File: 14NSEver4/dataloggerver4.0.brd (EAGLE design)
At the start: 80 x 25.4 mm, 44 parts, among them Q1 16mhz, SW2 SRIDE_SWITCH

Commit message: changed board files
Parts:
- removed C7: 3.3uF, rcl:C0603
- removed CON1, CON3: (no value), XR Connector:3PIN
- removed CON2, CON4, CON5: (no value), XR Connector:2PIN
- removed D1, D2: (no value), ChipDiodes:SOD-123
- removed DCDC1, DCDC3: (no value), DC-DC:5V1A_M78AR05-1
- removed DCDC2: (no value), DC-DC:3.3V1A_M78AR033-1
- removed IM2: IM920_IM920C, CANSAT12th:IM920_IM920C
- removed U$2, U$4, U$5: 2SJ681-PCH, mosfet:2SJ681
- removed U$6, U$7: 1X5, PinSocket:1X5
- removed U$8: ATMEGA328P-AU, ATMEGA328P-AU:QFP80P900X900X120-32N
- added BMX1, BMX2: BMX055, BMX055:BMX055
- added CN1, CN2: DM3AT, microSD:DM3AT
- added JP3, JP5, JP7: (no value), pinhead:1X05
- added JP4, JP6: (no value), pinhead:1X06
- added L3, L4: (no value), Chip LED:OSXX1608C1A
- added Q2: 16mhz, crystal:HC49UP
- added R16, R17, R18, R2, R3, R5, R6: 10k, rcl:R0603
- added U$1: ATMEGA328P-AU, ATMAGA328P-AU:QFP80P900X900X120-32N
- C4: value 3.3uF -> 22p
- C5: value 10uF -> 22p
- C6: value 3.3uF -> 0.1μ
- R10, R8: value 1k -> 10k
- R14, R15: value 4.7k -> 100
- R9: value 100k -> 10k
- SW2: value SRIDE_SWITCH -> (none); device Sride Switch:SRIDE_SWITCH -> Tact switch:TVAF06-A020B-R
- U$3: value 2SK4017-NCH -> ATMEGA328P-AU; device mosfet:2SK4017 -> ATMAGA328P-AU:QFP80P900X900X120-32N
- moved L1 89.2 mm to (67.3, 2.54), turned to 180 degrees
- moved R12 88.4 mm to (67.3, 5.08), turned to 180 degrees
- moved L2 57.8 mm to (63.5, 2.54)
- moved R13 54.5 mm to (63.5, 5.08)
- moved JP2 43.7 mm to (61.0, -2.54), turned to 0 degrees
- moved R4 43.6 mm to (73.7, 22.9)
- moved SW1 43.1 mm to (64.8, -10.2)
- moved C3 42.2 mm to (59.7, -11.4), turned to 90 degrees
- moved C5 40.7 mm to (59.7, -17.8)
- moved JP1 34.5 mm to (54.6, 22.9)
- moved Q1 33.6 mm to (21.6, -16.5)
- moved R11 32.0 mm to (62.2, 17.8)
- moved R10 29.2 mm to (55.9, -8.89), turned to 270 degrees
- moved C2 29.2 mm to (26.7, -11.4), turned to 0 degrees
- moved R8 28.0 mm to (62.2, 15.2), turned to 0 degrees
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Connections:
- removed net +5V1: DCDC1.VIN, U$5.DRAIN
- removed net FP: CON5.P$1, D2.C, R10.2, U$2.GATE, U$3.GATE, U$4.GATE
- removed net FP1: D1.C
- removed net FP_CHECKER: C5.1, R8.2, U$8.PD4
- removed net IM_BUSY: IM2.$P1, U$8.PD6
- removed net IM_RESET: IM2.$P19, U$8.PD5
- removed net LED: IM2.$P15
- removed net LED_1.0: U$8.PD2
- removed net RAW: CON2.P$2, U$2.SOURCE
- removed net RX_IM: IM2.$P6, U$8.PD7
- removed net SERVO1: CON1.P$1, R14.1, U$8.PC1
- removed net SERVO2: CON3.P$1, R15.1, U$8.PC0
- removed net SERVO5V: C7.1, CON1.P$2, CON3.P$2, DCDC3.VOUT
- removed net SERVORAW: CON4.P$2, D1.A, DCDC3.VIN
- removed net SW: R9.1, SW2.L, U$5.GATE
- removed net TX_IM: IM2.$P7
- removed net TX_RM: U$8.PB0
- new net 3V3: BMX1.3V3, BMX2.3V3
- new net GPSRX: JP6.4, U$3.PD6
- new net GPSTX: JP6.3, U$3.PD7
- new net LED1.2: R13.2, U$1.PD6
- new net LED1.3: R12.2, U$1.PD7
- new net MISO1: CN2.DAT0, JP4.4, R11.1, U$3.PB4MISO
- new net MOSI1: CN2.CMD, JP4.5, R8.1, U$3.PB3MOSI
- new net N$11: L3.AN, R14.1
- new net N$5: JP6.6
- new net RESET1: C6.2, JP5.3
- new net RESETB1: C6.1, JP4.6, R16.2, SW2.P$2, U$3.PC6RESET
- new net RST: JP6.5, U$3.PD5
- new net RX1: JP5.4, U$3.PD0RX
- new net SCK1: CN2.CLK, JP4.3, R9.1, U$3.PB5
- new net SCL1: BMX2.SCL, R18.2, U$3.PC5SCL
- new net SDA1: BMX2.SDA, R17.2, U$3.PC4SDA
- new net SS1: CN2.CD/DAT3, R5.1, U$3.PB2SS
- new net TX1: JP5.5, U$3.PD1TX
- new net VCCIO: BMX1.VCCIO, BMX2.VCCIO
- net +3V3: now also CN1.VDD, CN2.VDD, JP3.4, JP7.5, R1.2, R17.1, R18.1, R2.2, R3.2, R5.2, R6.2, R7.2, R8.2, R9.2; no longer C6.1, DCDC2.VOUT, IM2.$P17, U$3.DRAIN, U$6.P$2, U$7.P$1
- net +5V: now also BMX1.VCC, BMX2.VCC, JP3.3, JP4.1, JP5.1, JP6.1, JP7.4, R10.1, R16.1, U$1.AVCC, U$1.VCC, U$1.VCC2, U$3.AVCC, U$3.VCC, U$3.VCC2; no longer C4.1, DCDC1.VOUT, DCDC2.VIN, R1.1, R14.2, R15.2, U$6.P$3, U$7.P$2, U$8.AVCC, U$8.VCC1, U$8.VCC2
- net BORD1: now also JP3.1, U$1.PD3; no longer U$6.P$5, U$8.PD3
- net BORD2: now also JP3.5, U$1.PD2; no longer U$6.P$1, U$8.PB1
- net BORDRX: now also JP7.3, U$3.PC3; no longer U$7.P$3, U$8.PC3
- net BORDTX: now also JP7.2, U$3.PC2; no longer U$7.P$4, U$8.PC2
- net GND: now also BMX1.GND, BMX2.GND, CN1.VSS, CN2.VSS, JP3.2, JP4.2, JP5.2, JP6.2, JP7.1, L3.CT, L4.CT, SW2.P$1, U$1.GND, U$1.GND2, U$1.GND3, U$3.GND, U$3.GND2, U$3.GND3; no longer C6.2, C7.2, CON1.P$3, CON2.P$1, CON3.P$3, CON4.P$1, CON5.P$2, DCDC1.GND, DCDC2.GND, DCDC3.GND, IM2.$P18, R10.1, R7.1, SW2.LR, U$6.P$4, U$7.P$5, U$8.GND1, U$8.GND2, U$8.GND3
- net LED1.0: now also R15.2, U$3.PD2; no longer R13.2
- net LED1.1: now also R14.2, U$3.PD3; no longer R12.2
- net MISO: now also CN1.DAT0, R7.1, U$1.PB4MISO; no longer U$8.PB4
- net MOSI: now also CN1.CMD, R3.1, U$1.PB3MOSI; no longer U$8.PB3
- net N$12: now also U$1.PB6; no longer U$8.PB6
- net N$13: now also U$1.PB7; no longer U$8.PB7
- net N$14: now also C5.1, Q2.2, U$3.PB7; no longer R7.2, R8.1, U$3.SOURCE
- net N$2: now also L4.AN, R15.1; no longer U$2.DRAIN, U$4.DRAIN
- net N$3: now also C4.1, Q2.1, U$3.PB6; no longer D2.A, R9.2, U$4.SOURCE, U$5.SOURCE
- net RESETB: now also R10.2, U$1.PC6RESET; no longer R1.2, U$8.PC6
- net RX: now also U$1.PD0RX; no longer U$8.PD0
- net SCK: now also CN1.CLK, R6.1, U$1.PB5; no longer U$8.PB5
- net SCL: now also BMX1.SCL, R4.1, U$1.PC5SCL; no longer R11.1, U$8.PC5
- net SDA: now also BMX1.SDA, R2.1, U$1.PC4SDA; no longer R4.1, U$8.PC4
- net SS: now also CN1.CD/DAT3, R1.1, U$1.PB2SS; no longer U$8.PB2
- net TX: now also U$1.PD1TX; no longer U$8.PD1
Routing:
- net +5V: track 27.7 -> 0.00 mm

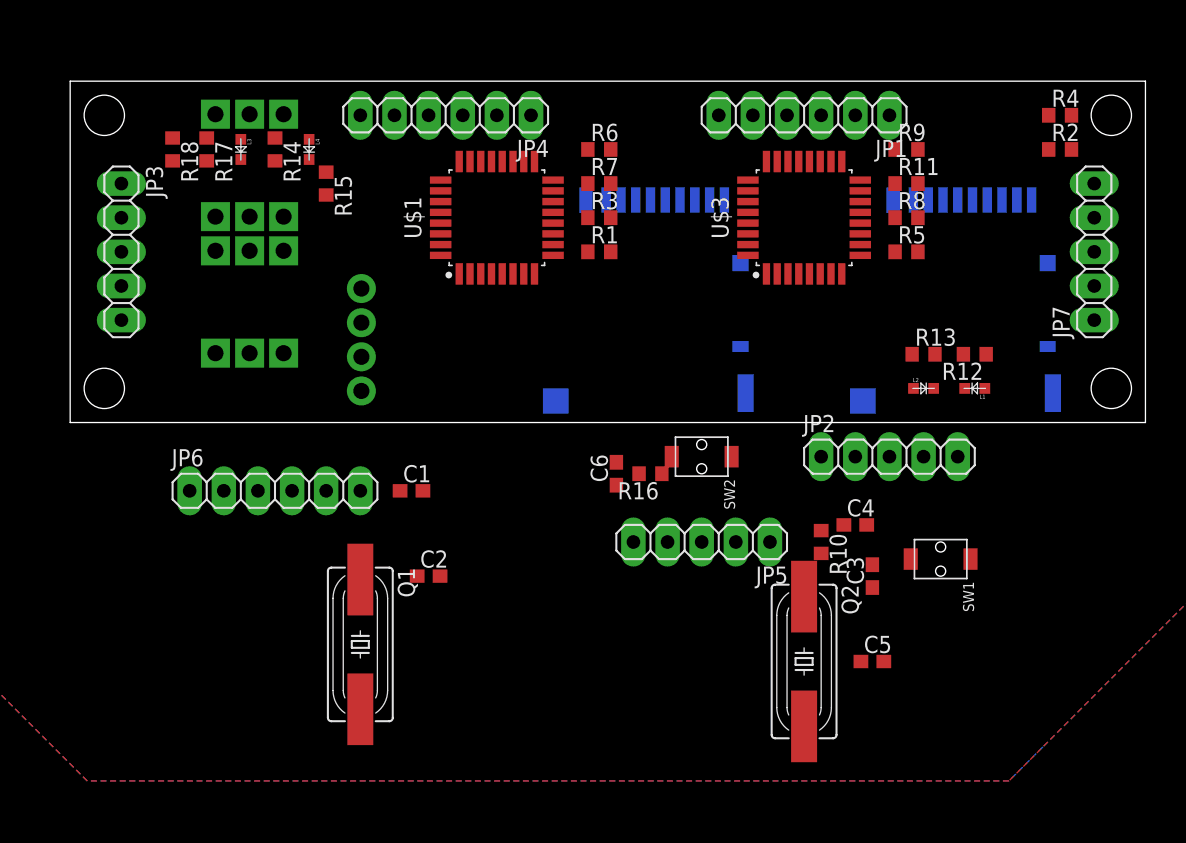
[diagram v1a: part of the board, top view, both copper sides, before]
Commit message: Changed board file
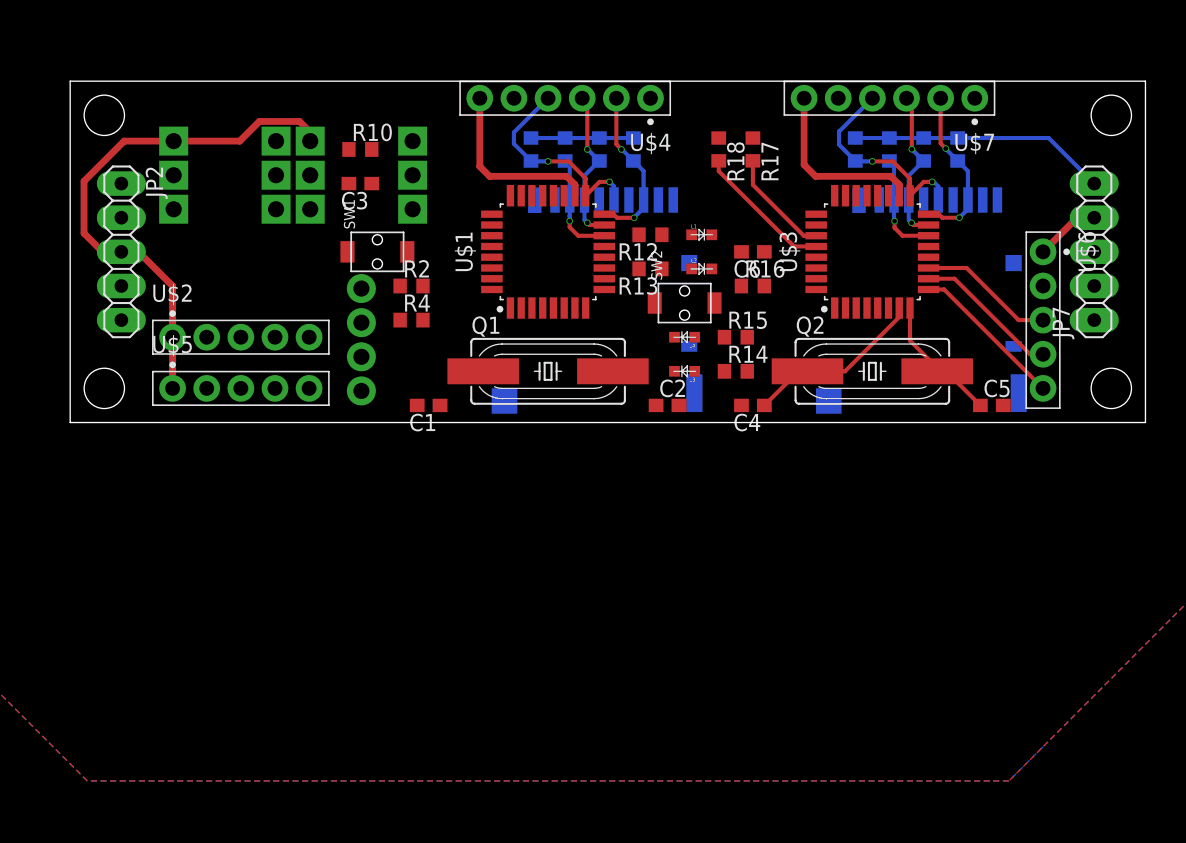
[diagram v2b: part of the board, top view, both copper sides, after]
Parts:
- removed JP1, JP4, JP6: (no value), pinhead:1X06
- removed JP3, JP5: (no value), pinhead:1X05
- added U$2, U$5, U$6: 1X5, pin_socket:HDRVR5W64P254_1X5_1310X250X865B
- added U$4, U$7: 1X61X6_2.5, pin_socket:HDRVR6W64P254_1X6_1564X250X865B
- moved JP2 59.1 mm to (3.81, 12.7), turned to 270 degrees
- moved R4 50.6 mm to (25.4, 7.62)
- moved R2 49.3 mm to (25.4, 10.2)
- moved C3 48.0 mm to (21.6, 17.8), turned to 180 degrees
- moved SW1 47.7 mm to (22.9, 12.7), turned to 90 degrees
- moved R10 45.0 mm to (21.6, 20.3), turned to 0 degrees
- moved R17 40.6 mm to (50.8, 20.3)
- moved R18 40.6 mm to (48.3, 20.3)
- moved R14 38.1 mm to (49.5, 3.81), turned to 0 degrees
- moved L3 36.9 mm to (45.7, 3.81), turned to 180 degrees
- moved R15 32.6 mm to (49.5, 6.35), turned to 0 degrees
- moved L4 31.2 mm to (45.7, 6.35), turned to 180 degrees
- moved R12 25.7 mm to (43.2, 14.0)
- moved Q1 24.7 mm to (35.6, 3.81), turned to 0 degrees
- moved L1 23.3 mm to (47.0, 14.0), turned to 0 degrees
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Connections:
- removed net N$5: JP6.6
- net +3V3: now also JP2.4; no longer JP3.4
- net +5V: now also JP2.3, U$2.1, U$4.6, U$5.1, U$6.1, U$7.6; no longer JP1.1, JP2.1, JP3.3, JP4.1, JP5.1, JP6.1
- net BORD1: now also JP2.1; no longer JP3.1
- net BORD2: now also JP2.5; no longer JP3.5
- net GND: now also U$2.2, U$4.5, U$5.2, U$6.2, U$7.5; no longer JP1.2, JP3.2, JP4.2, JP5.2, JP6.2
- net GPSRX: now also U$6.4; no longer JP6.4
- net GPSTX: now also U$6.3; no longer JP6.3
- net MISO: now also U$4.2; no longer JP1.4
- net MISO1: now also U$7.2; no longer JP4.4
- net MOSI: now also U$4.3; no longer JP1.5
- net MOSI1: now also U$7.3; no longer JP4.5
- net RESET: now also U$2.3; no longer JP2.3
- net RESET1: now also U$5.3; no longer JP5.3
- net RESETB: now also U$4.1; no longer JP1.6
- net RESETB1: now also U$7.1; no longer JP4.6
- net RST: now also U$6.5; no longer JP6.5
- net RX: now also U$2.4; no longer JP2.4
- net RX1: now also U$5.4; no longer JP5.4
- net SCK: now also U$4.4; no longer JP1.3
- net SCK1: now also U$7.4; no longer JP4.3
- net TX: now also U$2.5; no longer JP2.5
- net TX1: now also U$5.5; no longer JP5.5
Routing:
- net +5V: track 0.00 -> 71.2 mm
- net +3V3: track 0.00 -> 26.8 mm
- net SCK: track 0.00 -> 15.8 mm, vias 0 -> 2
- net SCK1: track 0.00 -> 15.8 mm, vias 0 -> 2
- net N$3: track 0.00 -> 13.4 mm
- net MISO1: track 0.00 -> 12.4 mm, vias 0 -> 2
- net MISO: track 0.00 -> 12.4 mm, vias 0 -> 2
- net MOSI: track 0.00 -> 11.7 mm, vias 0 -> 2
- net MOSI1: track 0.00 -> 11.7 mm, vias 0 -> 2
- net RST: track 0.00 -> 11.6 mm
- net GPSRX: track 0.00 -> 10.8 mm
- net SCL1: track 0.00 -> 10.3 mm
- net GPSTX: track 0.00 -> 10.1 mm
- net N$14: track 0.00 -> 9.92 mm
- net SDA1: track 0.00 -> 8.07 mm
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
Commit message: Changed board
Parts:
- moved SW2 9.16 mm to (50.8, 16.5), turned to 270 degrees
- moved SW1 1.80 mm to (21.6, 14.0), turned to 0 degrees
- moved C6 1.27 mm to (50.8, 14.0)
- moved R16 1.27 mm to (50.8, 11.4)
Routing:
- net +5V: track 71.2 -> 217.4 mm, vias 0 -> 6
- net RX1: track 0.00 -> 104.7 mm, vias 0 -> 1
- net TX1: track 0.00 -> 95.4 mm, vias 0 -> 1
- net RESET1: track 0.00 -> 77.1 mm, vias 0 -> 4
- net +3V3: track 26.8 -> 100.8 mm, vias 0 -> 3
- net RESETB: track 0.00 -> 72.2 mm, vias 0 -> 5
- net BORDTX: track 0.00 -> 38.4 mm, vias 0 -> 2
- net BORD2: track 0.00 -> 36.6 mm, vias 0 -> 1
- net BORD1: track 0.00 -> 36.4 mm, vias 0 -> 2
- net RESETB1: track 0.00 -> 35.0 mm, vias 0 -> 2
- net BORDRX: track 0.00 -> 33.7 mm, vias 0 -> 2
- net SDA1: track 8.07 -> 40.1 mm, vias 0 -> 1
- net SCL: track 0.00 -> 31.8 mm
- net SCL1: track 10.3 -> 41.0 mm, vias 0 -> 1
- net SDA: track 0.00 -> 27.4 mm
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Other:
- board size 80 x 25.4 mm -> 82.5 x 27.9 mm
